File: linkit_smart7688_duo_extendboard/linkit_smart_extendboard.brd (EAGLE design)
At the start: 96.5 x 67.9 mm, 27 parts, among them U1 BME280

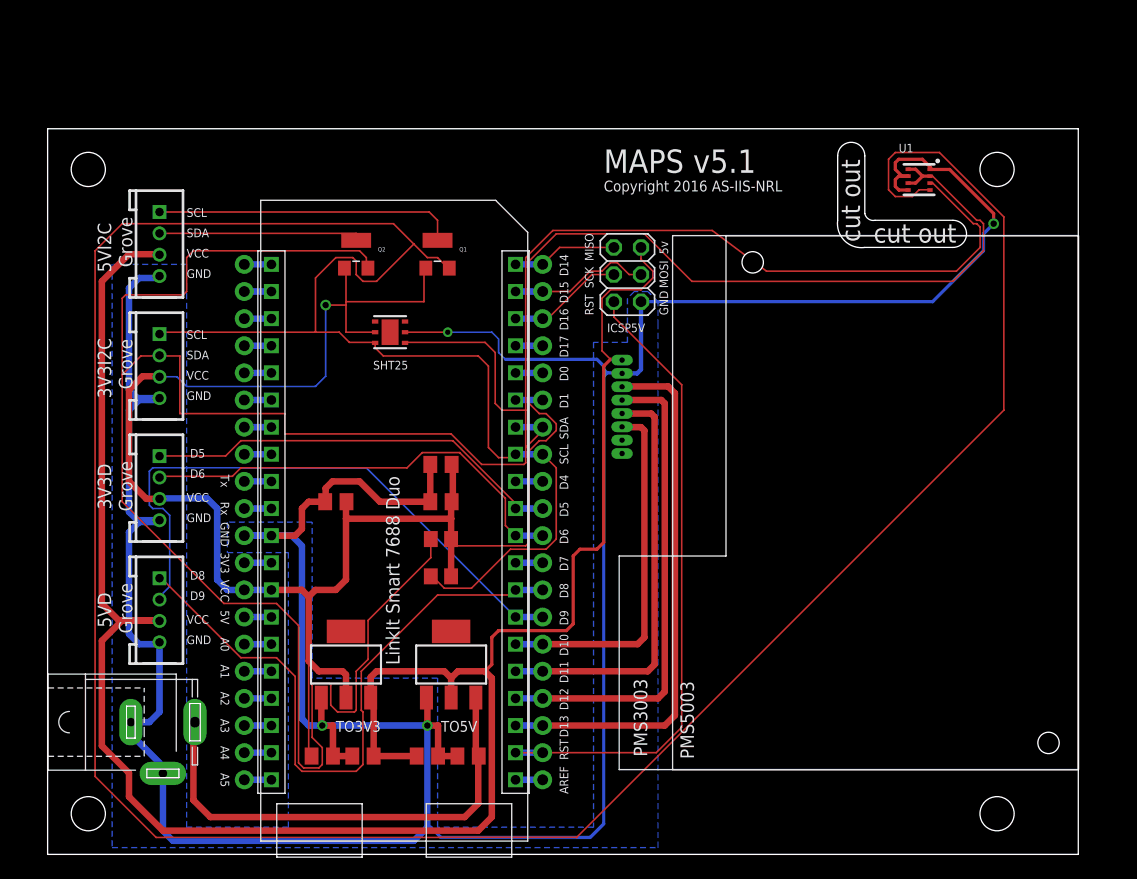
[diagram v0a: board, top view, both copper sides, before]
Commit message: update PCB layout,prepare for future box design
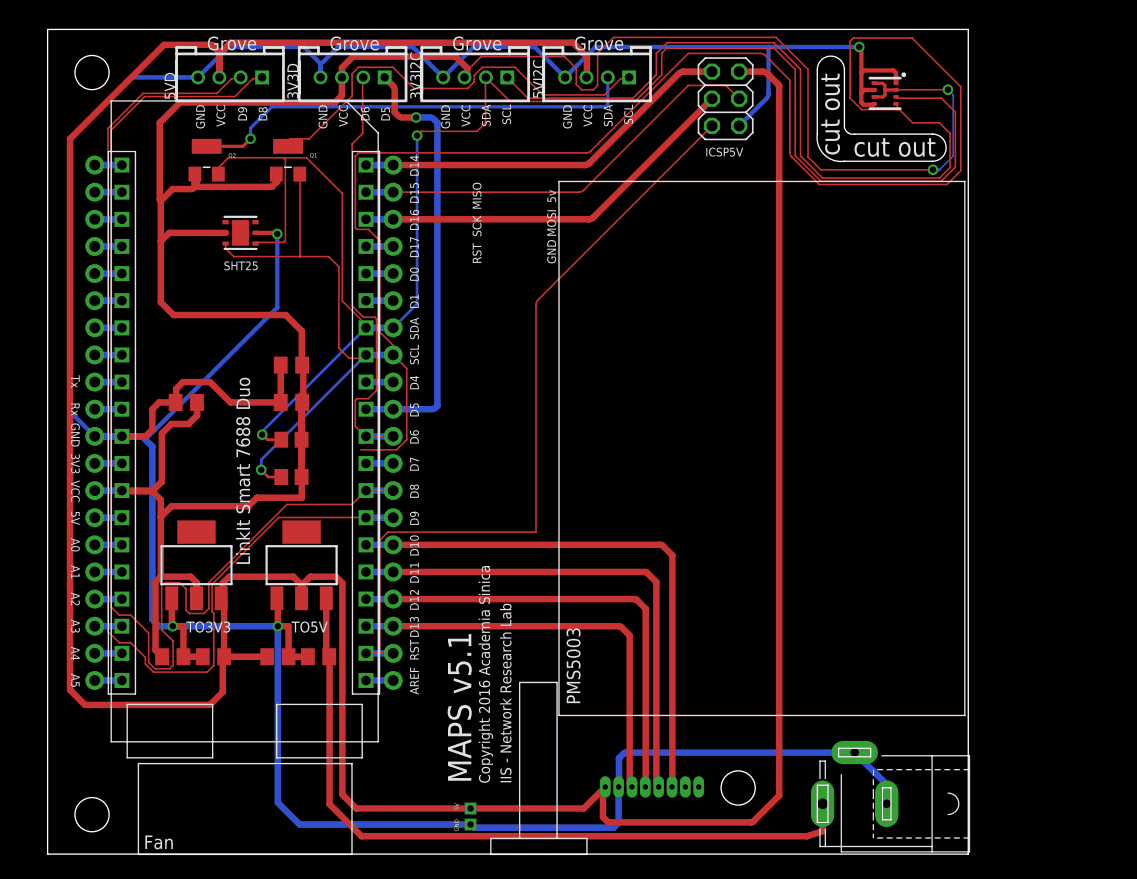
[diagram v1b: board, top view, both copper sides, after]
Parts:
- added U$5: (no value), fan_2_2:FAN
- added U$6: (no value), sma:SMA
- U$4: value (none) -> PIN2MM; device G3:G3 -> pin_2mm:PIN2MM
- moved POWER 65.2 mm to (75.6, 4.74), turned to 180 degrees
- moved U$4 57.5 mm to (39.1, 4.80), turned to 270 degrees
- moved 5VD 50.3 mm to (17.1, 72.8), turned to 180 degrees
- moved 5VI2C 43.8 mm to (51.5, 72.8), turned to 180 degrees
- moved 3V3D 42.5 mm to (28.6, 72.8), turned to 180 degrees
- moved 3V3I2C 40.1 mm to (40.0, 72.8), turned to 180 degrees
- moved PMS3003 36.2 mm to (56.6, 5.87), turned to 0 degrees
- moved ICSP5V 18.9 mm to (63.5, 70.8)
- moved C1 16.8 mm to (21.6, 18.5)
- moved C3 16.8 mm to (11.7, 18.5)
- moved C4 16.8 mm to (15.5, 18.5)
- moved L 16.8 mm to (4.42, 40.4)
- moved R 16.8 mm to (32.4, 40.4)
- moved R3 16.8 mm to (22.8, 38.8)
- moved R4 16.8 mm to (22.8, 35.3)
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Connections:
- net +5V: now also U$4.5V
- net GND: now also U$4.GND
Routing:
- net SDA: track 259.3 -> 156.7 mm, vias 0 -> 2
- net +5V: track 194.1 -> 293.3 mm
- net SCL: track 314.8 -> 251.4 mm, vias 0 -> 1
- net N$33: track 60.7 -> 111.6 mm
- net N$30: track 56.5 -> 103.4 mm
- net N$22: track 13.3 -> 39.5 mm
- net N$23: track 10.9 -> 37.0 mm
- net N$21: track 9.87 -> 35.9 mm
- net B$1: track 45.5 -> 69.6 mm
- net N$39: track 19.1 -> 42.3 mm, vias 0 -> 1
- net N$2: track 33.9 -> 50.8 mm
- net N$34: track 61.6 -> 75.4 mm
- net N$36: track 28.2 -> 40.9 mm
- net N$35: track 50.7 -> 39.3 mm
- net +3V3: track 232.7 -> 242.2 mm, vias 1 -> 2
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- removed copper zone on layer 16, net GND
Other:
- board size 96.5 x 67.9 mm -> 86.2 x 77.2 mm
- board text added: "Copyright 2016 Academia Sinica"
- board text added: "IIS - Network Research Lab"
- board text removed: "Copyright 2016 AS-IIS-NRL"

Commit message: modify PCB layout to fit the RP1135C box and add RP1135C drafting pdf
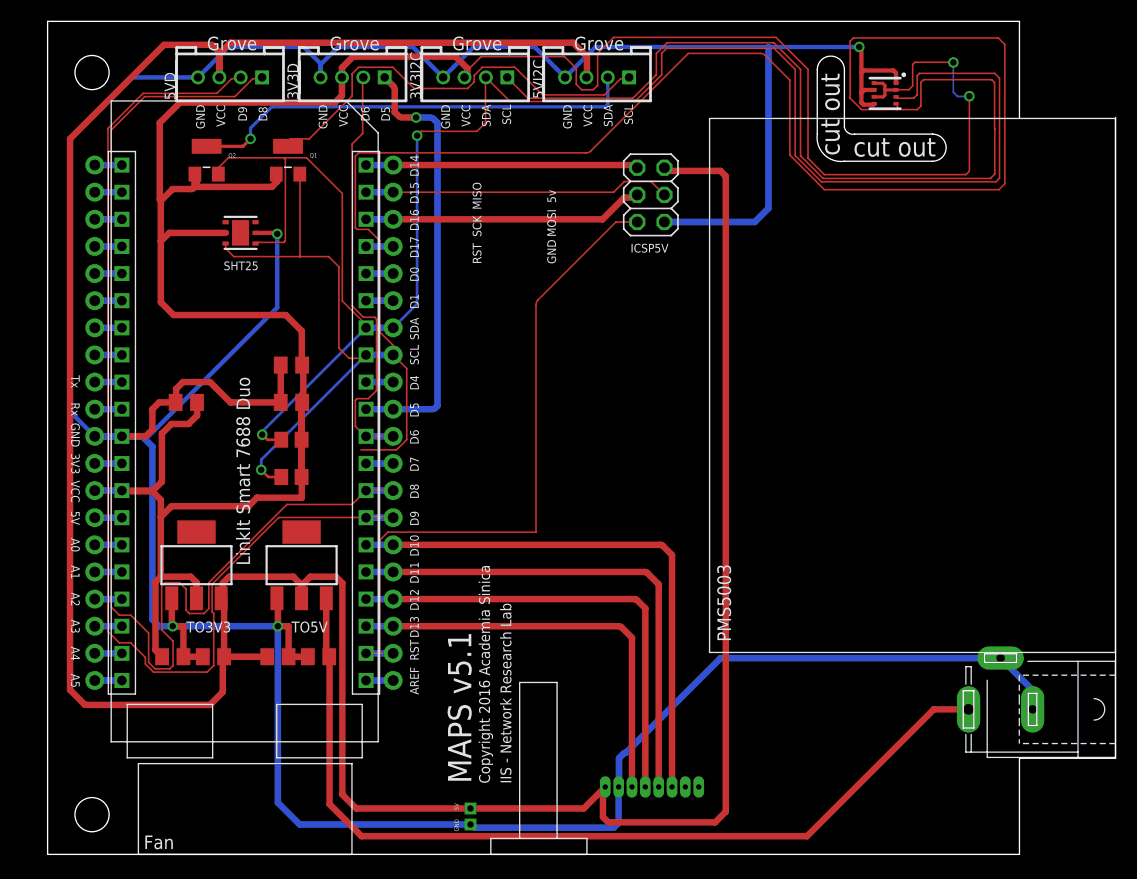
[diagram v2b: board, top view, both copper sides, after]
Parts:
- moved POWER 16.3 mm to (89.2, 13.6)
- moved U$2 15.3 mm to (100.0, 18.9)
- moved ICSP5V 11.4 mm to (56.5, 61.8)
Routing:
- net GND: track 322.4 -> 356.6 mm
- net SCL: track 251.4 -> 278.3 mm
- net B$1: track 69.6 -> 85.6 mm
- net SDA: track 156.7 -> 170.5 mm
- net +5V: track 293.3 -> 282.6 mm
- net N$34: track 75.4 -> 64.7 mm
- net N$23: track 37.0 -> 26.3 mm
- net N$22: track 39.5 -> 28.9 mm
- net N$21: track 35.9 -> 25.5 mm
- net +3V3: track 242.2 -> 251.4 mm
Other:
- board size 86.2 x 77.2 mm -> 100 x 78 mm

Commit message: update PCB layout for RP1135C box
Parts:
- removed Q1, Q2: (no value), adafruit:SOT23-W
- added BSS138N_01, BSS138N_02: (no value), adafruit:SOT23-W
- U$1: device linkit7688:LINKIT7688 -> linkit_smart_extendboard:LINKIT7688
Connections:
- net +3V3: now also BSS138N_01.1, BSS138N_02.1; no longer Q1.1, Q2.1
- net N$36: now also BSS138N_01.3; no longer Q1.3
- net N$39: now also BSS138N_02.3; no longer Q2.3
- net SCL: now also BSS138N_01.2; no longer Q1.2
- net SDA: now also BSS138N_02.2; no longer Q2.2
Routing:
- net SDA: track 170.5 -> 166.7 mm
- net SCL: track 278.3 -> 276.5 mm
- net N$36: track 40.9 -> 42.5 mm
- net GND: track 356.6 -> 355.5 mm
- net +3V3: track 251.4 -> 252.2 mm

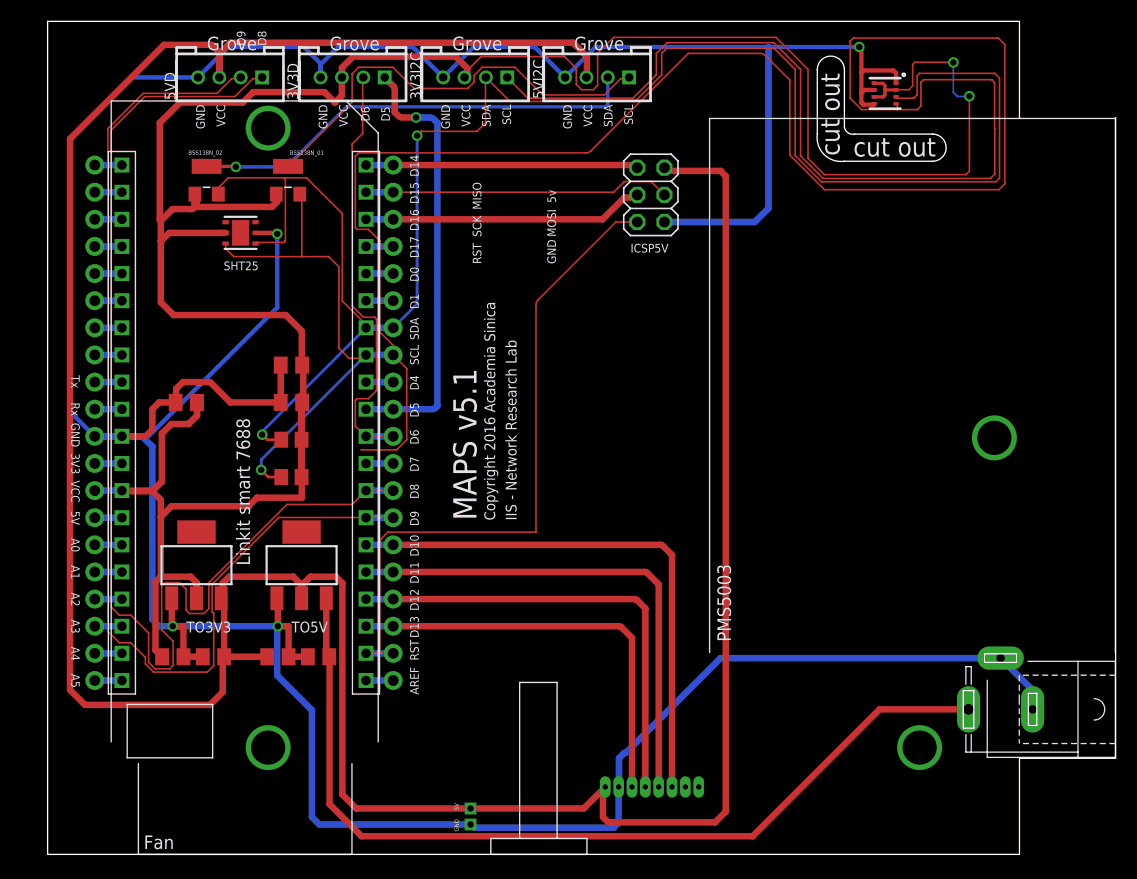
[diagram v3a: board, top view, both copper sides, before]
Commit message: update PCB layout & RP1135C piercing 3D design
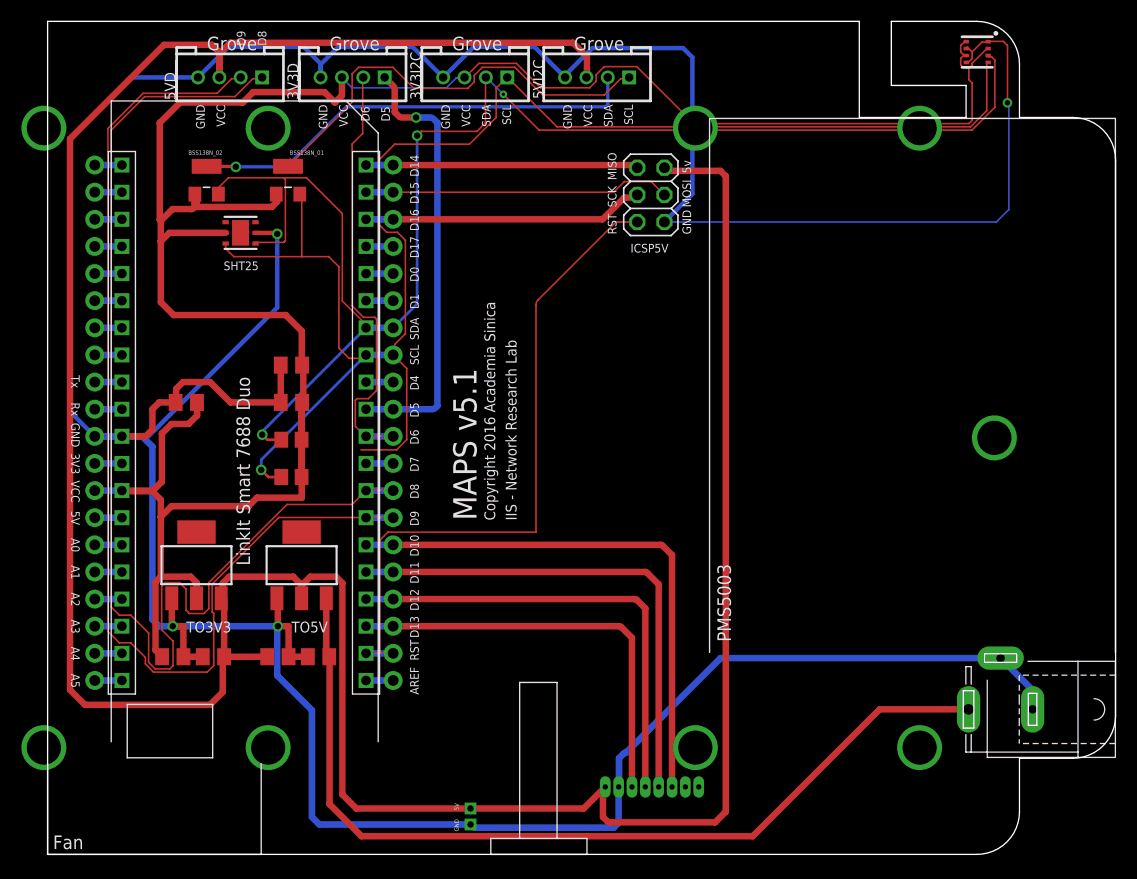
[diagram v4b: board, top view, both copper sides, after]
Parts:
- U$1: device linkit_smart_extendboard:LINKIT7688 -> linkit7688:LINKIT7688
- moved U1 9.46 mm to (87.0, 75.1)
- moved U$5 8.50 mm to (0.00, 0.00)
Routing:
- net SCL: track 276.5 -> 151.7 mm
- net SDA: track 166.7 -> 139.0 mm, vias 2 -> 3
- net +3V3: track 252.2 -> 227.7 mm, vias 2 -> 0
- net GND: track 355.5 -> 373.4 mm
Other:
- outline, holes or cut-outs redrawn
- board text removed: "cut out"

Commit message: update PCB layout & RP1135C piercing 3D design
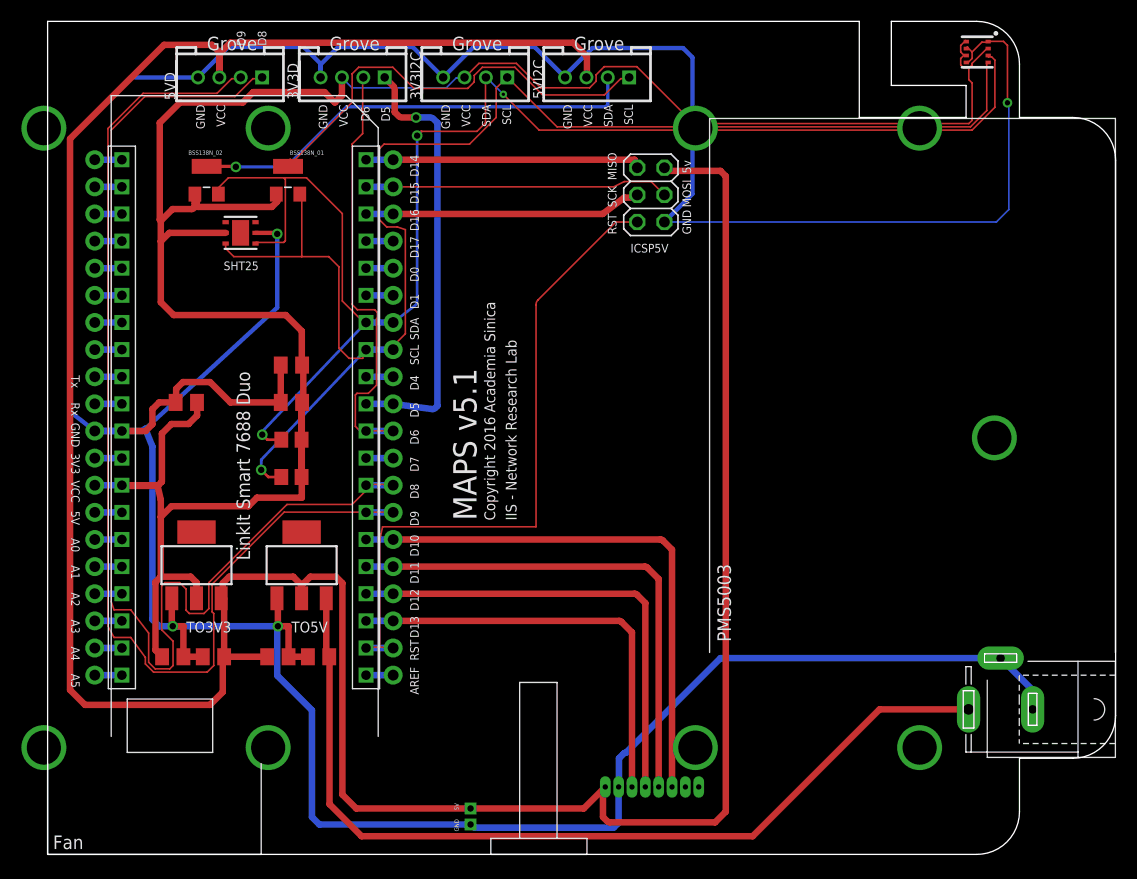
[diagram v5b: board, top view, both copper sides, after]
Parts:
- moved L 0.50 mm to (4.42, 40.9)
- moved R 0.50 mm to (32.4, 40.9)
- moved U$1 0.50 mm to (6.96, 65.0)
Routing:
- net SCL: track 151.7 -> 140.7 mm
- net GND: track 373.4 -> 372.6 mm
- net N$33: track 111.6 -> 112.2 mm
- net N$38: track 43.3 -> 43.8 mm
- net N$35: track 39.7 -> 40.2 mm
- net N$29: track 47.2 -> 47.7 mm
- net N$2: track 50.8 -> 51.3 mm

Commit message: change BME280 position to another side, flip the G5 and change position, change DC position
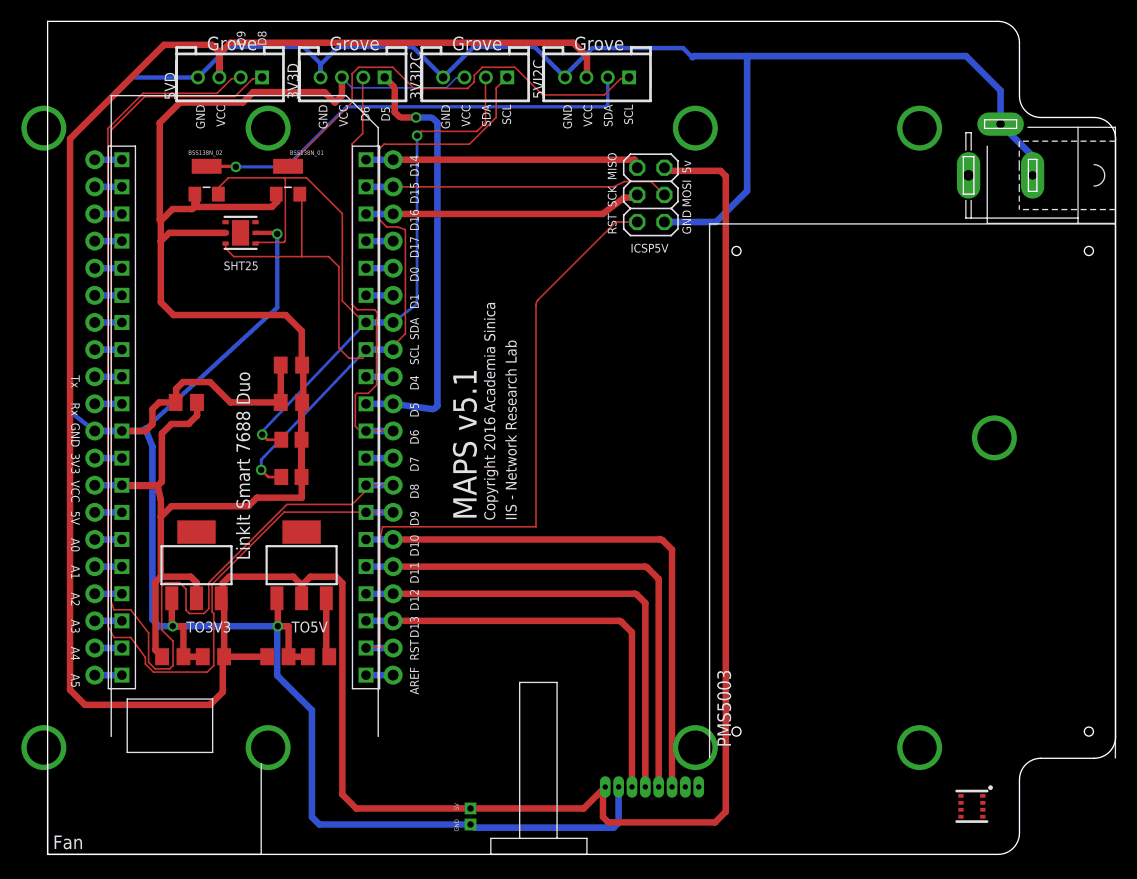
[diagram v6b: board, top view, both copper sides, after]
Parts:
- moved U1 70.6 mm to (86.5, 4.50)
- moved POWER 50.0 mm to (89.2, 63.6)
- moved U$2 9.87 mm to (100.0, 9.03)
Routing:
- net B$1: track 85.6 -> 5.75 mm
- net +3V3: track 228.2 -> 163.8 mm
- net GND: track 372.6 -> 314.8 mm, vias 4 -> 3
- net SDA: track 138.9 -> 83.0 mm, vias 3 -> 2
- net SCL: track 140.7 -> 88.7 mm
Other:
- outline, holes or cut-outs redrawn

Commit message: update PCB layout & RP1135C piercing 3D design
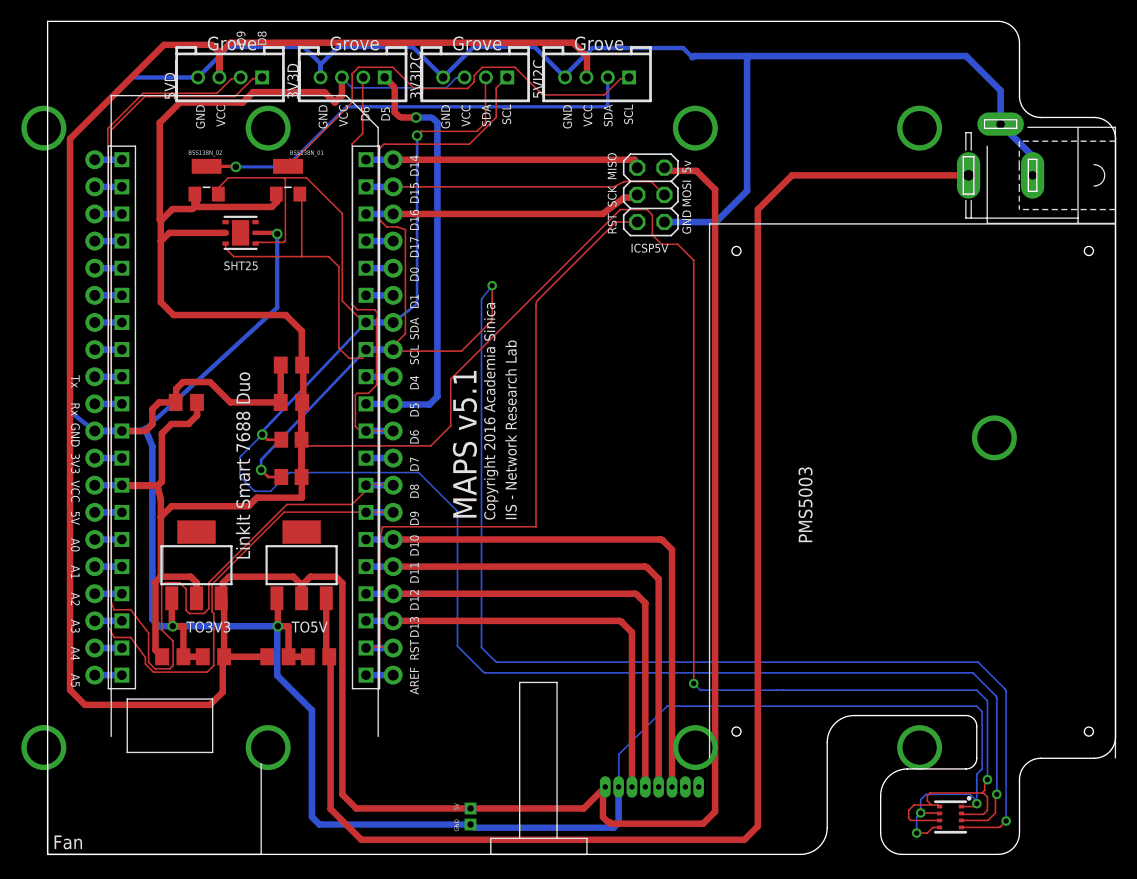
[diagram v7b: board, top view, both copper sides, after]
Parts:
- moved U1 2.24 mm to (84.5, 3.50)
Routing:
- net +3V3: track 163.8 -> 310.1 mm, vias 0 -> 2
- net B$1: track 5.75 -> 140.6 mm
- net SCL: track 88.7 -> 204.0 mm, vias 1 -> 3
- net SDA: track 83.0 -> 190.3 mm, vias 2 -> 3
- net GND: track 314.8 -> 377.7 mm, vias 3 -> 6
- net +5V: track 282.6 -> 280.0 mm
- net N$10: track 41.3 -> 40.7 mm
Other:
- outline, holes or cut-outs redrawn
